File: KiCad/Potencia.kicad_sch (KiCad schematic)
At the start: 64 parts, among them J1 Conn_01x02, J11 Conn_01x02, J12 Conn_01x02, J3-4 Conn_01x02, J5 Conn_01x02, J7-8 Conn_01x02, J9 Conn_01x02, K1 G6E, K10 G6E, K2 G6E, K3 G6E, K4 G6E, K5 G6E, K6 G6E, K7 G6E, K8 G6E, K9 G6E, Q1 NMOS, Q10 NMOS, Q11 IRLZ44N, Q12 IRLZ44N, Q2 NMOS, Q3 NMOS, Q4 NMOS, Q5 NMOS, Q6 NMOS, Q7 NMOS, Q8 NMOS, Q9 NMOS, U4 ${SIM.PARAMS}, U5 ${SIM.PARAMS}

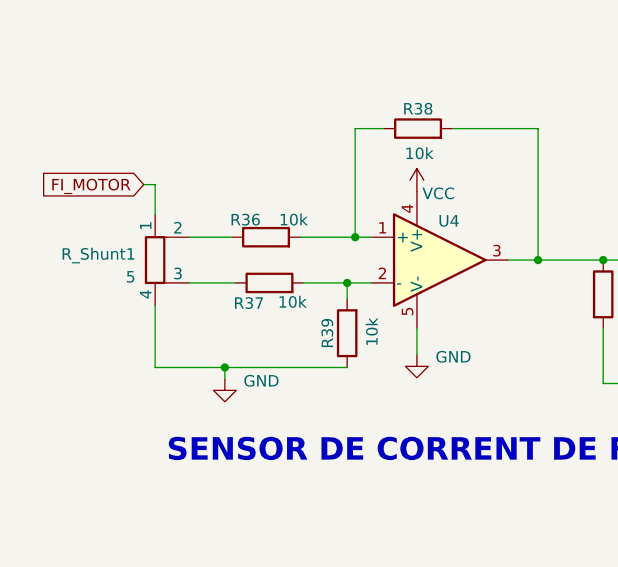
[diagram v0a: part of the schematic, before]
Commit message: Enrotament Part digital finalitzada
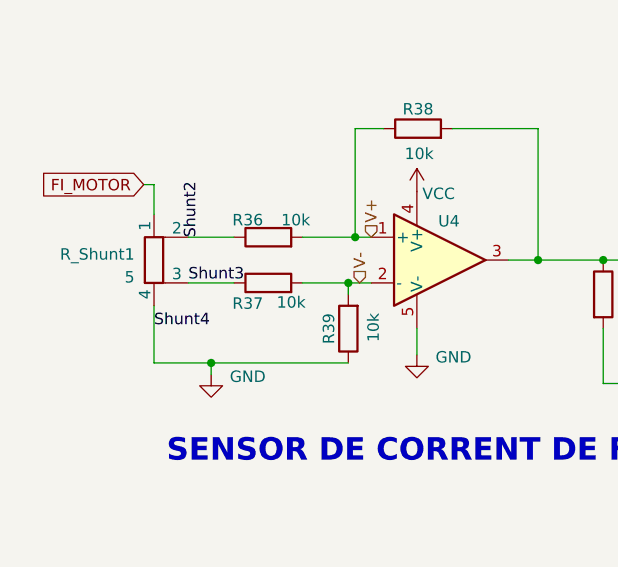
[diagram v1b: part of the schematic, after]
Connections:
- net Shunt2: now reaches R36.1, R_Shunt1.2
- net Shunt3: now reaches R37.1, R_Shunt1.3
- net V+: now reaches R36.2, R38.1, U4.1 (+)
- net V-: now reaches R37.2, R39.2, U4.2 (-)
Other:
- moved on the sheet: R39
